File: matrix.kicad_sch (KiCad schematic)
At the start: 225 parts

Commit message: added capacitors for LEDs and annotatios
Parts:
- removed D? (x17): D, symbol Device:D_Small
- removed SW? (x17): SW_HS, marbastlib-mx:SW_MX_HS_1u, symbol marbastlib-mx:MX_SW_HS
- gave numbers to parts that had none: 191

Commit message: added footprints to compontents
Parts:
- D1, D10, D11, D12, D13, D14, D15, D16, D17, D18, D19, D2, D20, D21, D22, D23, D24, D25, D26, D27, D28, D29, D3, D30, D31, D32, D33, D34, D35, D36, D37, D38, D39, D4, D40, D41, D42, D43, D44, D45, D46, D47, D48, D49, D5, D50, D51, D52, D53, D54, D55, D56, D57, D58, D59, D6, D60, D61, D62, D63, D64, D65, D66, D67, D68, D69, D7, D70, D71, D72, D73, D74, D75, D76, D77, D78, D79, D8, D80, D81, D82, D83, D84, D85, D86, D87, D88, D89, D9, D90: footprint (none) -> Diode_SMD:D_SOD-123

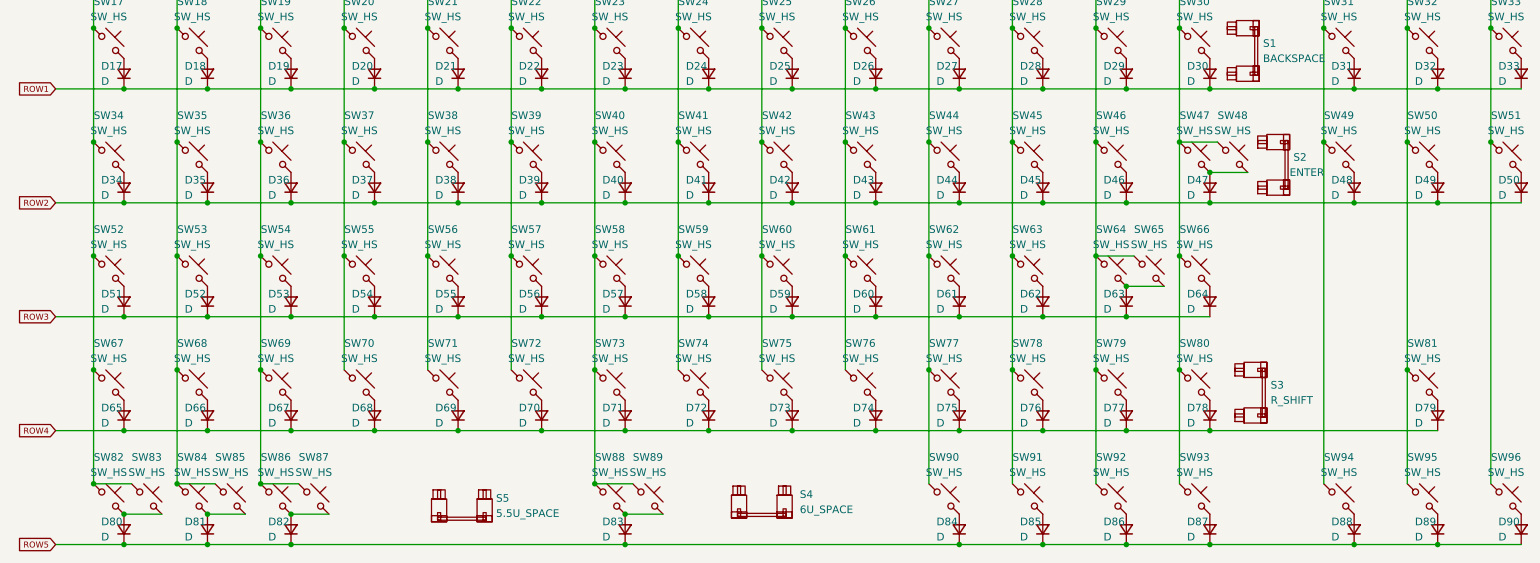
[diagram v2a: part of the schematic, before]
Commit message: loaded and fipped footprints to pcb editor
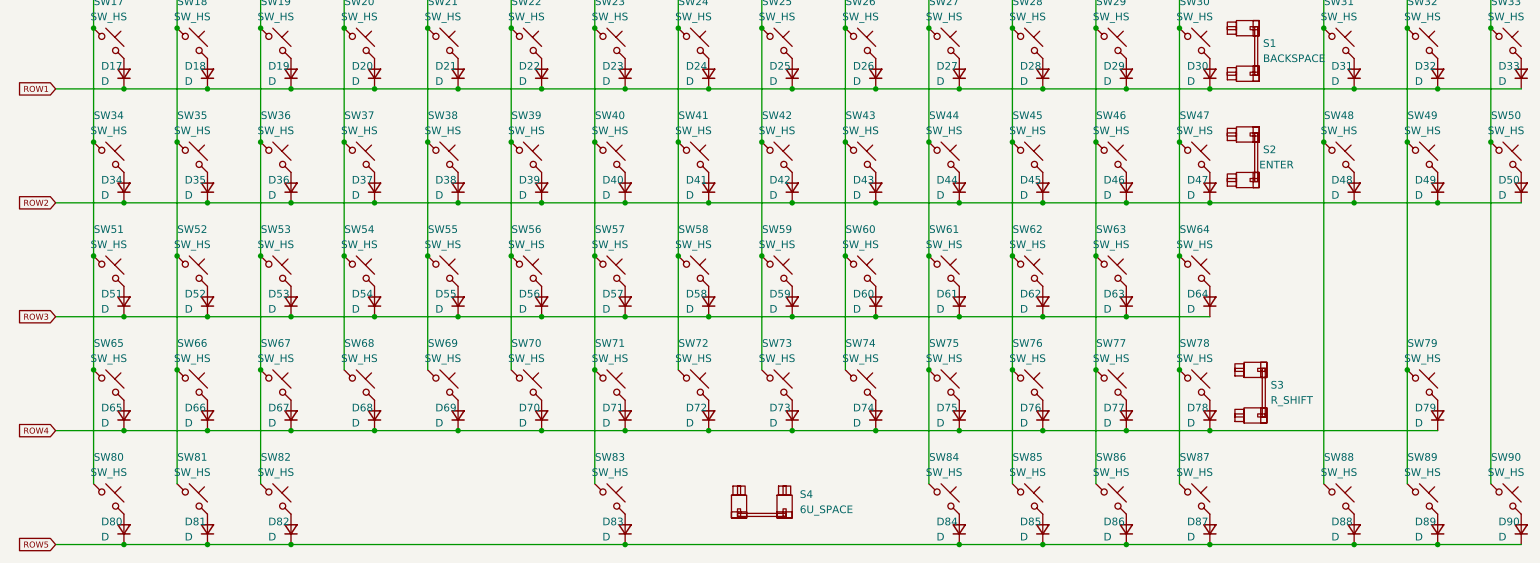
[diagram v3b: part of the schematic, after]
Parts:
- removed S5: 5.5U_SPACE, marbastlib-mx:STAB_MX_P_6.25u, symbol marbastlib-mx:MX_stab
- removed SW48, SW65, SW83, SW85, SW87, SW89: SW_HS, marbastlib-mx:SW_MX_HS_1u, symbol marbastlib-mx:MX_SW_HS
- S1: footprint marbastlib-mx:STAB_MX_P_6.25u -> marbastlib-mx:STAB_MX_2u
- S2: footprint marbastlib-mx:STAB_MX_P_6.25u -> marbastlib-mx:STAB_MX_ISO_FLIPPED
- S3: footprint marbastlib-mx:STAB_MX_P_6.25u -> marbastlib-mx:STAB_MX_2.75u
- S4: footprint marbastlib-mx:STAB_MX_P_6.25u -> marbastlib-mx:STAB_MX_6u
- SW34: footprint marbastlib-mx:SW_MX_HS_1u -> marbastlib-mx:SW_MX_HS_1.5u
- SW51: renamed from SW52; footprint marbastlib-mx:SW_MX_HS_1u -> marbastlib-mx:SW_MX_HS_1.75u
- SW65: renamed from SW67; footprint marbastlib-mx:SW_MX_HS_1u -> marbastlib-mx:SW_MX_HS_1.25u
- SW80: renamed from SW82; footprint marbastlib-mx:SW_MX_HS_1u -> marbastlib-mx:SW_MX_HS_1.5u
- SW82: renamed from SW86; footprint marbastlib-mx:SW_MX_HS_1u -> marbastlib-mx:SW_MX_HS_1.5u
- SW84: renamed from SW90; footprint marbastlib-mx:SW_MX_HS_1u -> marbastlib-mx:SW_MX_HS_1.5u
- SW87: renamed from SW93; footprint marbastlib-mx:SW_MX_HS_1u -> marbastlib-mx:SW_MX_HS_1.5u
- renumbered SW49 to SW48, SW50 to SW49, SW51 to SW50, SW53 to SW52, SW54 to SW53, SW55 to SW54, SW56 to SW55, SW57 to SW56, SW58 to SW57, SW59 to SW58, SW60 to SW59, SW61 to SW60, SW62 to SW61, SW63 to SW62, SW64 to SW63, SW66 to SW64, SW68 to SW66, SW69 to SW67, SW70 to SW68, SW71 to SW69, SW72 to SW70, SW73 to SW71, SW74 to SW72, SW75 to SW73, SW76 to SW74, SW77 to SW75, SW78 to SW76, SW79 to SW77, SW80 to SW78, SW81 to SW79, SW84 to SW81, SW88 to SW83, SW91 to SW85, SW92 to SW86, SW94 to SW88, SW95 to SW89, SW96 to SW90
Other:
- moved on the sheet: S2

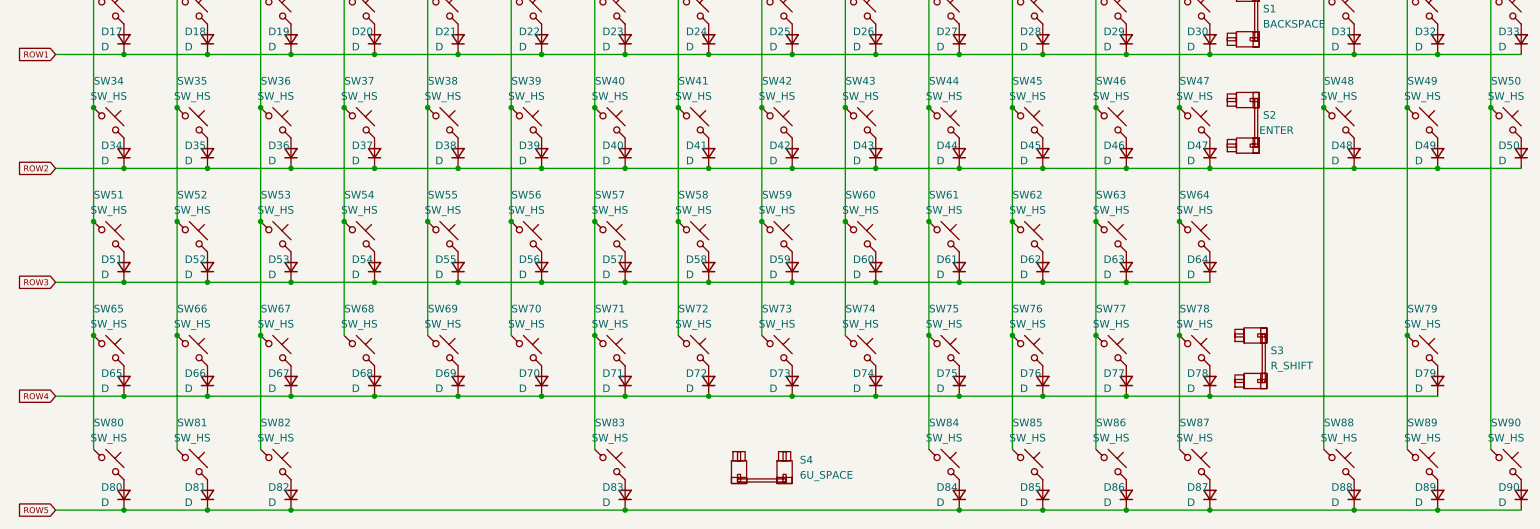
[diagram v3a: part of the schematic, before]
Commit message: placed switches and LEDs
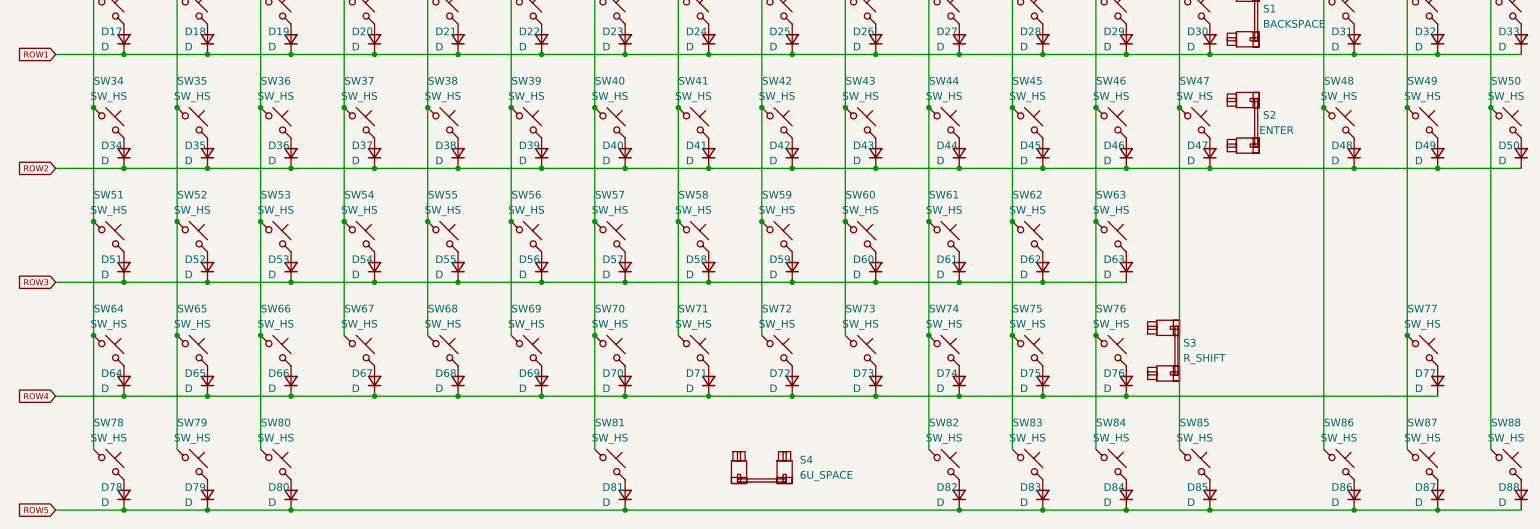
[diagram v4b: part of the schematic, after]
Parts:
- removed D64, D78: D, Diode_SMD:D_SOD-123, symbol Device:D_Small
- removed SW64, SW78: SW_HS, marbastlib-mx:SW_MX_HS_1u, symbol marbastlib-mx:MX_SW_HS
- renumbered D65 to D64, D66 to D65, D67 to D66, D68 to D67, D69 to D68, D70 to D69, D71 to D70, D72 to D71, D73 to D72, D74 to D73, D75 to D74, D76 to D75, D77 to D76, D79 to D77, D80 to D78, D81 to D79, D82 to D80, D83 to D81, D84 to D82, D85 to D83, D86 to D84, D87 to D85, D88 to D86, D89 to D87, D90 to D88, SW65 to SW64, SW66 to SW65, SW67 to SW66, SW68 to SW67, SW69 to SW68, SW70 to SW69, SW71 to SW70, SW72 to SW71, SW73 to SW72, SW74 to SW73, SW75 to SW74, SW76 to SW75, SW77 to SW76, SW79 to SW77, SW80 to SW78, SW81 to SW79, SW82 to SW80, SW83 to SW81, SW84 to SW82, SW85 to SW83, SW86 to SW84, SW87 to SW85, SW88 to SW86, SW89 to SW87, SW90 to SW88
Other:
- moved on the sheet: S3
